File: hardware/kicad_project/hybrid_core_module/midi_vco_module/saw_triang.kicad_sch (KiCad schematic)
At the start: 17 parts, among them U24 TL074

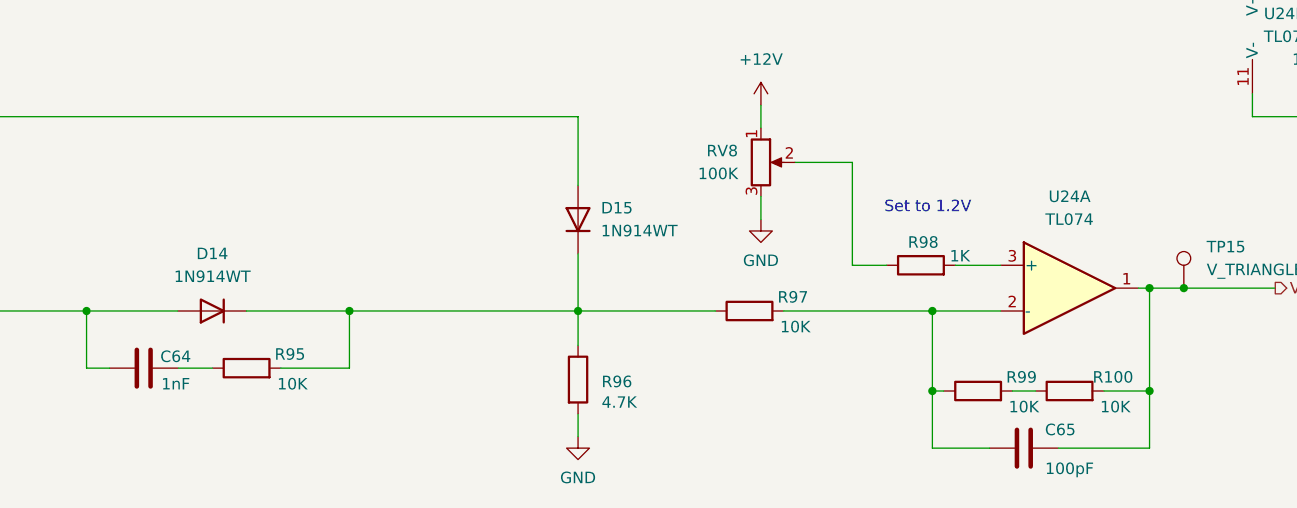
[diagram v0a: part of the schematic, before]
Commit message: Schematic updated. Components Footprint assignment started. Waiting for components mechanical validation before starting layout.
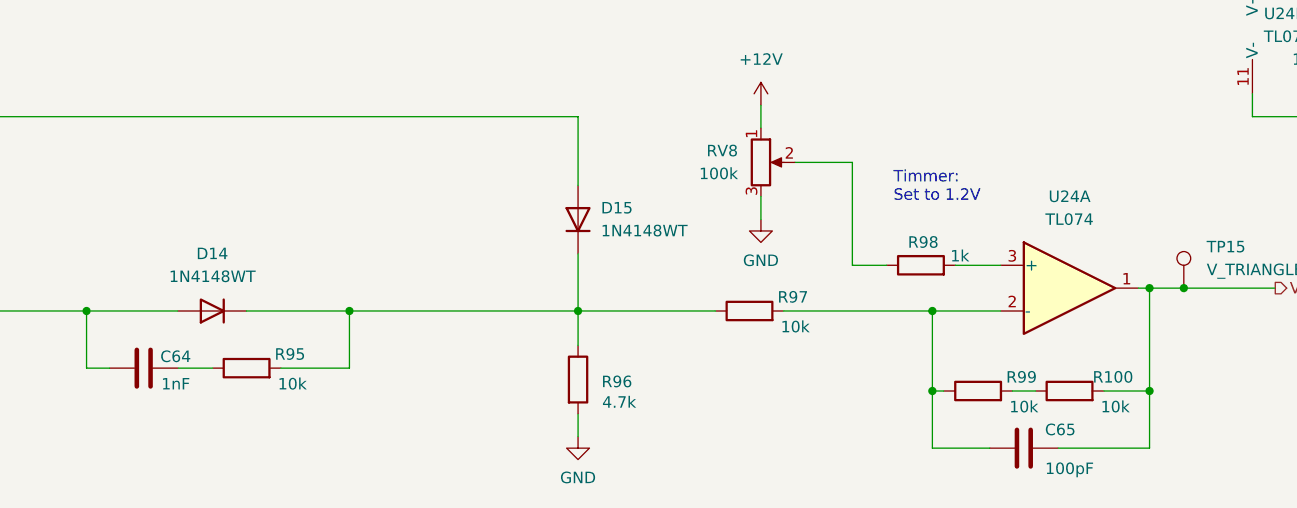
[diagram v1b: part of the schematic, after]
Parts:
- C1, C4: footprint (none) -> Capacitor_SMD:C_0402_1005Metric; Manufacturer (none) -> MURATA; Manufacturer PartNumer (none) -> GRM155R71E104KE14J
- C2, C3: footprint (none) -> Capacitor_SMD:C_0805_2012Metric; Manufacturer (none) -> MURATA; Manufacturer PartNumer (none) -> GRM219R71E105MA88J
- C64: Manufacturer (none) -> MURATA; Manufacturer PartNumer (none) -> GRM155R71E103KA01J
- C65: footprint (none) -> Capacitor_SMD:C_0402_1005Metric; Manufacturer (none) -> MURATA; Manufacturer PartNumer (none) -> GCM1555C1H101FA16J
- D14, D15: value 1N914WT -> 1N4148WT; Manufacturer (none) -> ONSEMI/FAIRCHILD; Manufacturer PartNumer (none) -> 1N4148WT
- R100, R95, R97, R99: value 10K -> 10k; footprint (none) -> Resistor_SMD:R_0402_1005Metric; Manufacturer (none) -> YAGEO; Manufacturer PartNumer (none) -> RT0402FRE0710KL
- R96: value 4.7K -> 4.7k; footprint (none) -> Resistor_SMD:R_0402_1005Metric; Manufacturer (none) -> YAGEO; Manufacturer PartNumer (none) -> RT0402FRE074K7L
- R98: value 1K -> 1k; footprint (none) -> Resistor_SMD:R_0402_1005Metric; Manufacturer (none) -> YAGEO; Manufacturer PartNumer (none) -> RT0402FRE071KL
- RV8: value 100K -> 100k; Manufacturer PartNumer (none) -> 3296X-104-LF
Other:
- note added: "Timmer: Set to 1.2V"
- note removed: "Set to 1.2V"

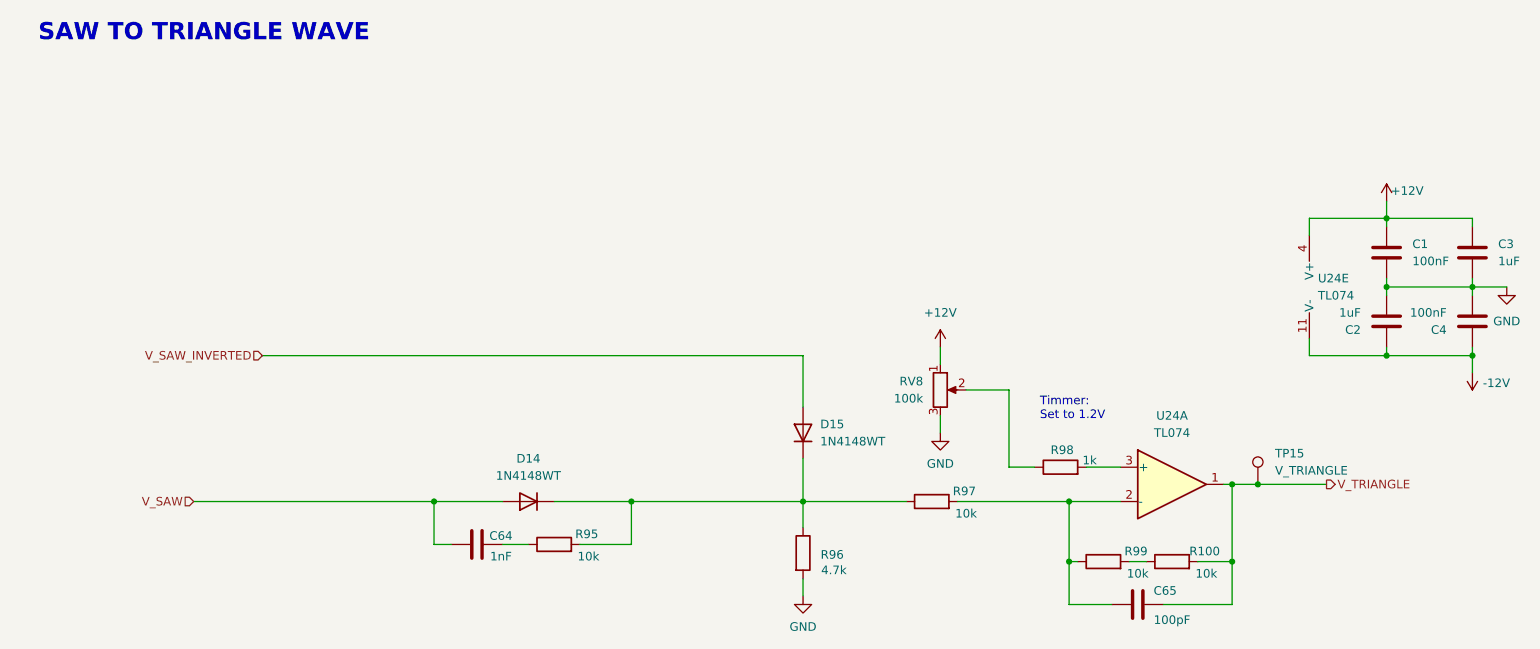
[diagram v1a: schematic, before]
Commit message: - schematic updated  - PN and footprints added
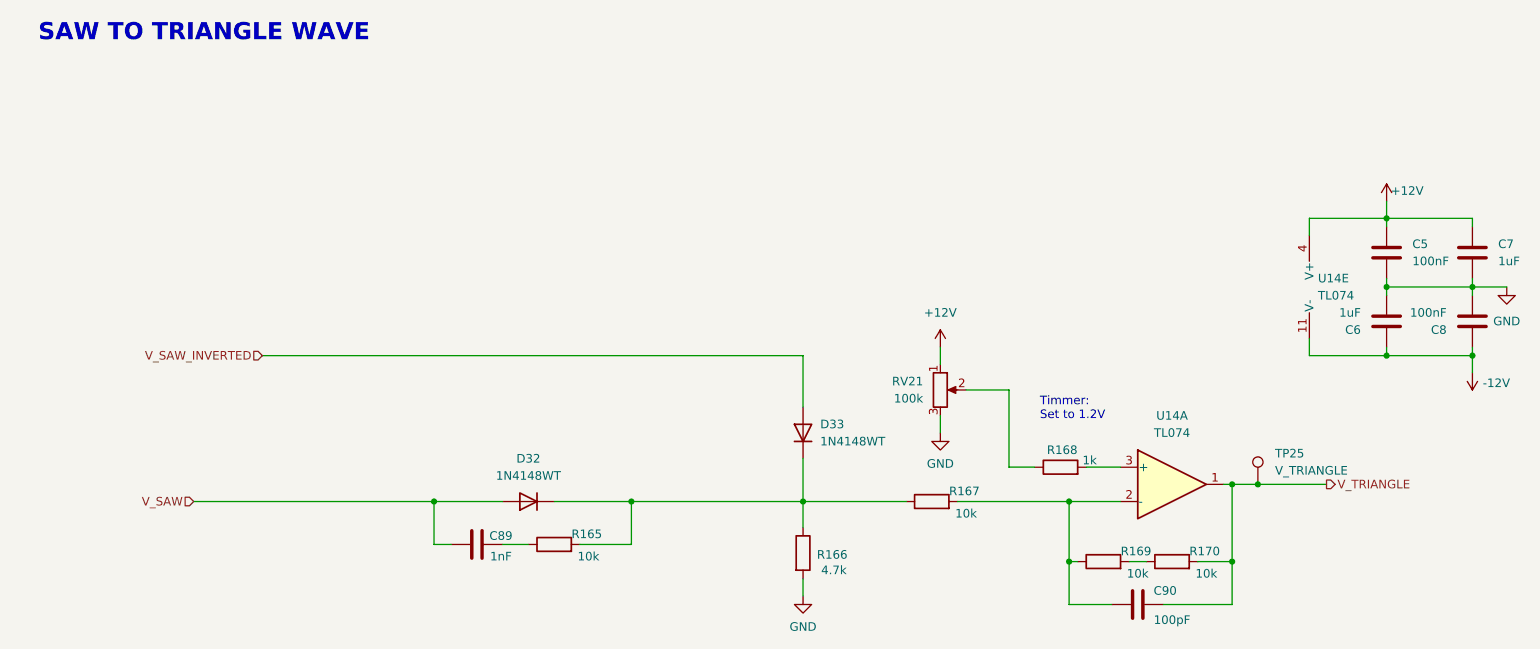
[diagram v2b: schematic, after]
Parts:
- RV21: renamed from RV8; footprint (none) -> Potentiometer_THT:Potentiometer_Bourns_3296W_Vertical; Manufacturer (none) -> KESHY; Manufacturer PartNumer 3296X-104-LF -> 3296W-104-LF
- U14: renamed from U24; footprint (none) -> Package_SO:SOIC-14_3.9x8.7mm_P1.27mm; Manufacturer (none) -> Texas Instruments
- renumbered C1 to C5, C2 to C6, C3 to C7, C4 to C8, C64 to C89, C65 to C90, D14 to D32, D15 to D33, R95 to R165, R96 to R166, R97 to R167, R98 to R168, R99 to R169, R100 to R170, TP15 to TP25

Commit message: components placement (interface) components placement per section
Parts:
- TP25: footprint (none) -> TestPoint:TestPoint_Pad_1.0x1.0mm
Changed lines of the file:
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@@
 			)
 		)
-		(property "Footprint" ""
+		(property "Footprint" "TestPoint:TestPoint_Pad_1.0x1.0mm"
 			(at 205.74 88.9 0)
 			(effects
